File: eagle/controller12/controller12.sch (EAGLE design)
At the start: 60 parts, among them IC1 ILD213T, J2 AVR_SPI_PRG_62X3_LOCK, Q1 FDD4141TO252, Q2 200mA/50V, Q3 FDD4141TO252, Q4 200mA/50V, Q5 200mA/50V, U3 MP2307, X1 1501_04, X2 ZX62D-B-5PA8

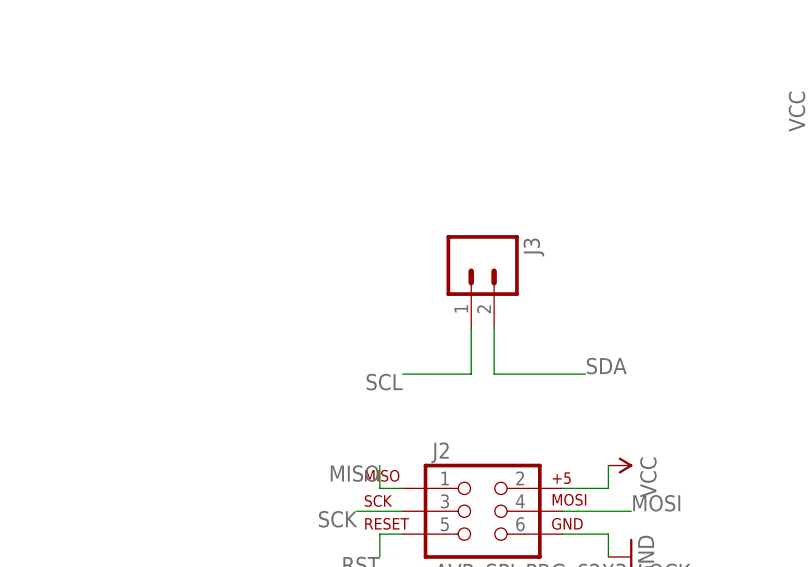
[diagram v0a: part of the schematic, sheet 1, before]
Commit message: controller12: added header for possible extension board
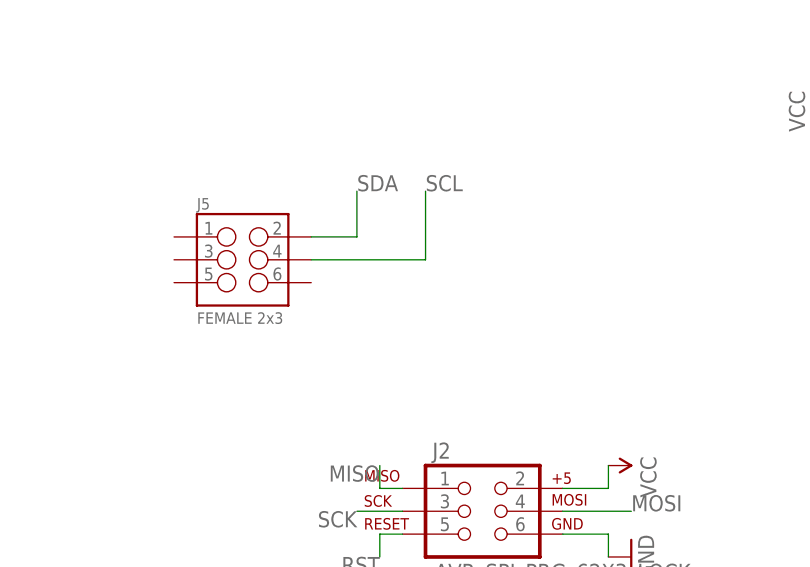
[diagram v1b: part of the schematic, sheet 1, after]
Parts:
- removed J3: (no value), SparkFun-Connectors:M02LOCK
- added J5: FEMALE 2x3, SparkFun-Connectors:M03X2FEMALE
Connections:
- net SCL: no longer J3.1
- net SDA: no longer J3.2
- net Z_GPIO_1: no longer J1.2
- net Z_GPIO_2: no longer J1.4
- net Z_GPIO_3: no longer J1.6
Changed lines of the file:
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@@
 <part name="S2" library="SparkFun-Electromechanical" deviceset="SWITCH-SPDT" device="SMD2"/>
 <part name="SUPPLY8" library="SparkFun-Aesthetics" deviceset="VCC" device=""/>
-<part name="J3" library="SparkFun-Connectors" deviceset="M02" device="LOCK"/>
+<part name="J5" library="SparkFun-Connectors" deviceset="M03X2" device="FEMALE" value="FEMALE 2x3"/>
 </parts>
 <sheets>
@@
 <instance part="S2" gate="1" x="162.56" y="106.68"/>
 <instance part="SUPPLY8" gate="G$1" x="147.32" y="106.68" rot="R90"/>
-<instance part="J3" gate="G$1" x="106.68" y="91.44" rot="R270"/>
+<instance part="J5" gate="G$1" x="81.28" y="91.44"/>
 </instances>
 <busses>
@@
 </segment>
 <segment>
-<wire x1="106.68" y1="78.74" x2="99.06" y2="78.74" width="0.1524" layer="91"/>
-<label x="99.06" y="78.74" size="1.778" layer="95" rot="R180"/>
-<pinref part="J3" gate="G$1" pin="1"/>
-<wire x1="106.68" y1="78.74" x2="106.68" y2="83.82" width="0.1524" layer="91"/>
+<wire x1="101.6" y1="91.44" x2="101.6" y2="99.06" width="0.1524" layer="91"/>
+<label x="101.6" y="99.06" size="1.778" layer="95"/>
+<wire x1="101.6" y1="91.44" x2="88.9" y2="91.44" width="0.1524" layer="91"/>
 </segment>
 </net>
@@
 </segment>
 <segment>
-<wire x1="109.22" y1="78.74" x2="119.38" y2="78.74" width="0.1524" layer="91"/>
-<label x="119.38" y="78.74" size="1.778" layer="95"/>
-<pinref part="J3" gate="G$1" pin="2"/>
-<wire x1="109.22" y1="78.74" x2="109.22" y2="83.82" width="0.1524" layer="91"/>
+<wire x1="93.98" y1="93.98" x2="93.98" y2="99.06" width="0.1524" layer="91"/>
+<label x="93.98" y="99.06" size="1.778" layer="95"/>
+<wire x1="93.98" y1="93.98" x2="88.9" y2="93.98" width="0.1524" layer="91"/>
 </segment>
 </net>
@@
 </segment>
 </net>
-<net name="Z_GPIO_1" class="0">
-<segment>
-<pinref part="J1" gate="G$1" pin="2"/>
-<wire x1="88.9" y1="73.66" x2="101.6" y2="73.66" width="0.1524" layer="91"/>
-<label x="101.6" y="73.66" size="1.778" layer="95"/>
-</segment>
-</net>
-<net name="Z_GPIO_2" class="0">
-<segment>
-<pinref part="J1" gate="G$1" pin="4"/>
-<wire x1="88.9" y1="71.12" x2="101.6" y2="71.12" width="0.1524" layer="91"/>
-<label x="101.6" y="71.12" size="1.778" layer="95"/>
-</segment>
-</net>
-<net name="Z_GPIO_3" class="0">
-<segment>
-<pinref part="J1" gate="G$1" pin="6"/>
-<wire x1="88.9" y1="68.58" x2="101.6" y2="68.58" width="0.1524" layer="91"/>
-<label x="101.6" y="68.58" size="1.778" layer="95"/>
-</segment>
-</net>

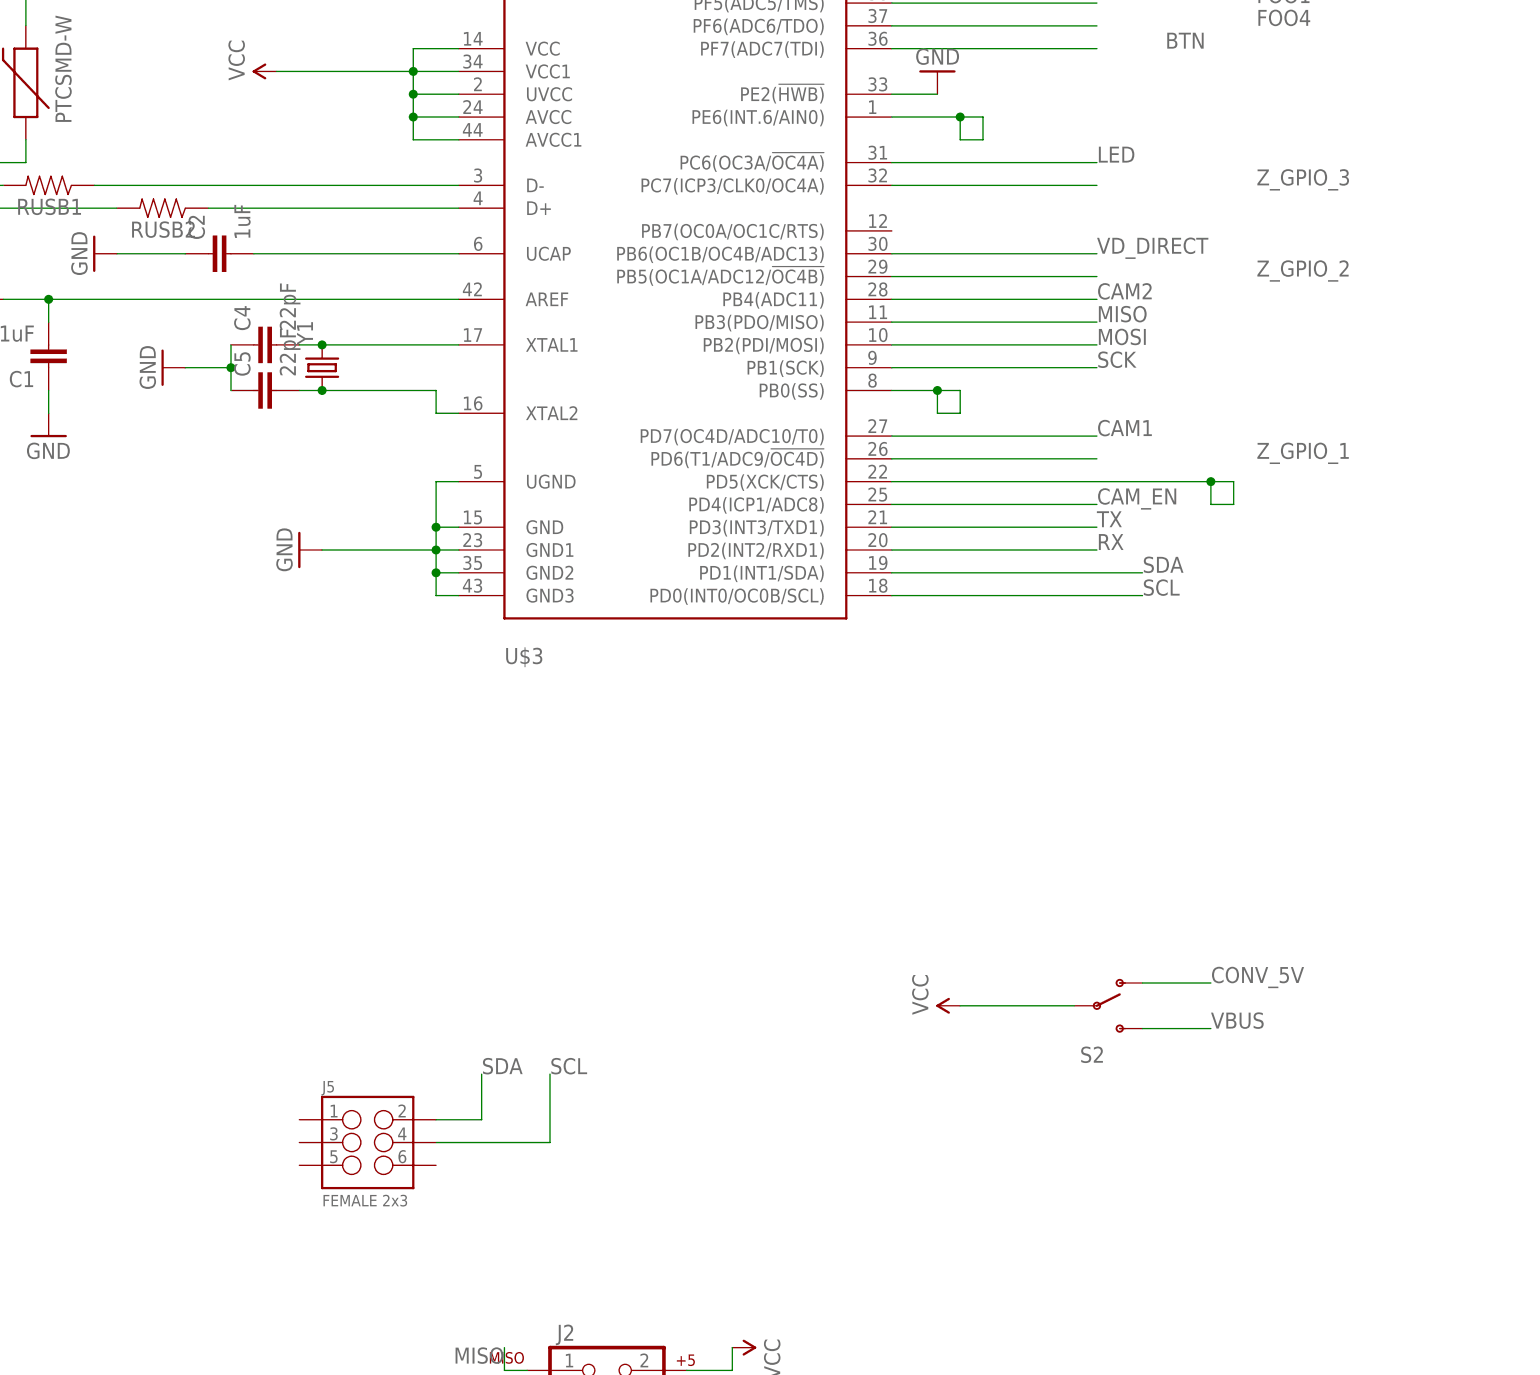
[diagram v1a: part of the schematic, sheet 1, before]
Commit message: controller12 routing improved
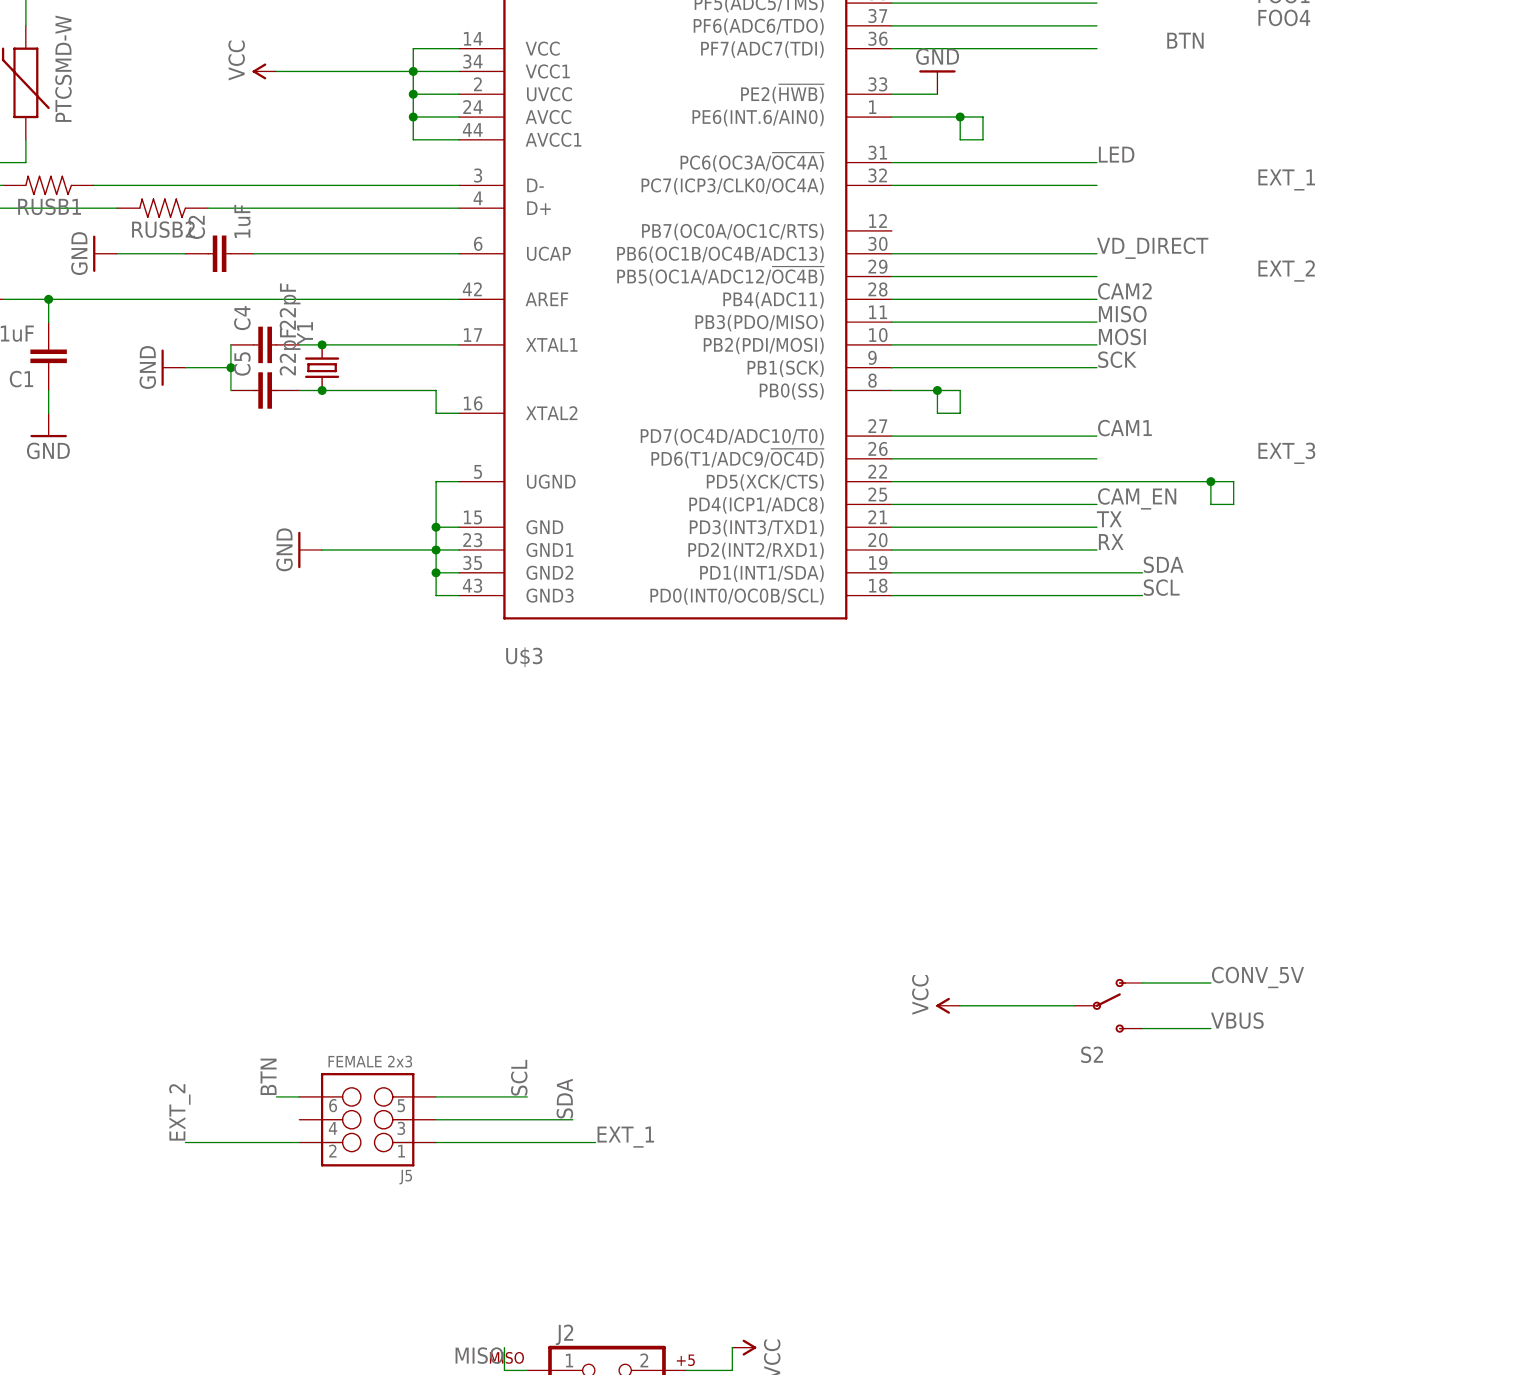
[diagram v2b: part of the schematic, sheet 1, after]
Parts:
- J4: device SparkFun-Connectors:M02LOCK -> SparkFun-Connectors:M02PTH
- S1: device SparkFun-Retired:TAC_SWITCHSMD -> SparkFun-Retired:TAC_SWITCHPTH
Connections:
- net Z_GPIO_1 renamed EXT_3
- removed net Z_GPIO_2: U$3.PB5(OC1A/ADC12/!OC4B)
- removed net Z_GPIO_3: U$3.PC7(ICP3/CLK0/OC4A)
- new net EXT_1: J5.1, U$3.PC7(ICP3/CLK0/OC4A)
- new net EXT_2: J5.2, U$3.PB5(OC1A/ADC12/!OC4B)
- net BTN: now also J5.6
- net SCL: now also J5.5
- net SDA: now also J5.3
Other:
- moved on the sheet: J5

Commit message: controller 12 progress zero_standalone enclosure
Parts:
- added D1: MBRS130LT3, diode:MBRS130LT3
- J2: value AVR_SPI_PRG_62X3_LOCK -> AVR_SPI_PRG_6PTH; device SparkFun-Connectors:AVR_SPI_PRG_62X3_LOCK -> SparkFun-Connectors:AVR_SPI_PRG_6PTH
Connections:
- removed net EXT_3: U$3.PD6(T1/ADC9/!OC4D)
- new net FOO5: U$3.PF7(ADC7(TDI)
- net BTN: now also J5.4, S1.4, U$3.PD6(T1/ADC9/!OC4D); no longer J5.6, S1.3, U$3.PF7(ADC7(TDI)
- net GND: now also J5.6
- net GNDA: now also D1.A
- net N$26: now also D1.C
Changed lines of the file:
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@@
 <part name="U$4" library="volzolib" deviceset="NANOFIT2" device=""/>
 <part name="U$5" library="volzolib" deviceset="NANOFIT2" device=""/>
-<part name="J2" library="SparkFun-Connectors" deviceset="AVR_SPI_PRG_6" device="2X3_LOCK"/>
+<part name="J2" library="SparkFun-Connectors" deviceset="AVR_SPI_PRG_6" device="PTH" value="AVR_SPI_PRG_6PTH"/>
 <part name="J4" library="SparkFun-Connectors" deviceset="M02" device="PTH"/>
 <part name="GND7" library="SparkFun-Aesthetics" deviceset="GND" device=""/>
@@
 <part name="SUPPLY8" library="SparkFun-Aesthetics" deviceset="VCC" device=""/>
 <part name="J5" library="SparkFun-Connectors" deviceset="M03X2" device="FEMALE" value="FEMALE 2x3"/>
+<part name="GND21" library="SparkFun-Aesthetics" deviceset="GND" device=""/>
+<part name="D1" library="diode" library_urn="urn:adsk.eagle:library:210" deviceset="MBRS130LT3" device="" package3d_urn="urn:adsk.eagle:package:43404/2"/>
+<part name="GND23" library="supply1" library_urn="urn:adsk.eagle:library:371" deviceset="GNDA" device=""/>
 </parts>
 <sheets>
@@
 <instance part="SUPPLY8" gate="G$1" x="147.32" y="106.68" rot="R90"/>
 <instance part="J5" gate="G$1" x="81.28" y="93.98" rot="R180"/>
+<instance part="GND21" gate="1" x="71.12" y="101.6" rot="R180"/>
 </instances>
 <busses>
@@
 <pinref part="GND29" gate="1" pin="GND"/>
 </segment>
+<segment>
+<pinref part="J5" gate="G$1" pin="6"/>
+<pinref part="GND21" gate="1" pin="GND"/>
+<wire x1="73.66" y1="96.52" x2="71.12" y2="96.52" width="0.1524" layer="91"/>
+<wire x1="71.12" y1="96.52" x2="71.12" y2="99.06" width="0.1524" layer="91"/>
+</segment>
 </net>
 <net name="RX" class="0">
@@
 <net name="BTN" class="0">
 <segment>
-<pinref part="S1" gate="S" pin="3"/>
 <pinref part="R5" gate="G$1" pin="2"/>
-<wire x1="58.42" y1="22.86" x2="66.04" y2="22.86" width="0.1524" layer="91"/>
 <wire x1="66.04" y1="22.86" x2="76.2" y2="22.86" width="0.1524" layer="91"/>
+<label x="76.2" y="22.86" size="1.778" layer="95"/>
+<pinref part="S1" gate="S" pin="4"/>
+<wire x1="58.42" y1="20.32" x2="63.5" y2="20.32" width="0.1524" layer="91"/>
+<wire x1="63.5" y1="20.32" x2="63.5" y2="22.86" width="0.1524" layer="91"/>
+<wire x1="63.5" y1="22.86" x2="66.04" y2="22.86" width="0.1524" layer="91"/>
 <junction x="66.04" y="22.86"/>
-<label x="76.2" y="22.86" size="1.778" layer="95"/>
-</segment>
-<segment>
-<pinref part="U$3" gate="G$1" pin="PF7(ADC7(TDI)"/>
-<wire x1="139.7" y1="213.36" x2="162.56" y2="213.36" width="0.1524" layer="91"/>
-<label x="170.18" y="213.36" size="1.778" layer="95"/>
-</segment>
-<segment>
-<pinref part="J5" gate="G$1" pin="6"/>
-<wire x1="73.66" y1="96.52" x2="71.12" y2="96.52" width="0.1524" layer="91"/>
-<label x="71.12" y="96.52" size="1.778" layer="95" rot="R90"/>
+</segment>
+<segment>
+<pinref part="U$3" gate="G$1" pin="PD6(T1/ADC9/!OC4D)"/>
+<wire x1="139.7" y1="167.64" x2="162.56" y2="167.64" width="0.1524" layer="91"/>
+<label x="180.34" y="167.64" size="1.778" layer="95"/>
+</segment>
+<segment>
+<pinref part="J5" gate="G$1" pin="4"/>
+<wire x1="73.66" y1="93.98" x2="66.04" y2="93.98" width="0.1524" layer="91"/>
+<label x="66.04" y="93.98" size="1.778" layer="95" rot="R90"/>
 </segment>
 </net>
@@
 </segment>
 </net>
-<net name="EXT_3" class="0">
-<segment>
-<pinref part="U$3" gate="G$1" pin="PD6(T1/ADC9/!OC4D)"/>
-<wire x1="139.7" y1="167.64" x2="162.56" y2="167.64" width="0.1524" layer="91"/>
-<label x="180.34" y="167.64" size="1.778" layer="95"/>
-</segment>
-</net>
 <net name="VBUS" class="0">
 <segment>
@@
 <wire x1="139.7" y1="187.96" x2="162.56" y2="187.96" width="0.1524" layer="91"/>
 <label x="180.34" y="187.96" size="1.778" layer="95"/>
+</segment>
+</net>
+<net name="FOO5" class="0">
+<segment>
+<pinref part="U$3" gate="G$1" pin="PF7(ADC7(TDI)"/>
+<wire x1="139.7" y1="213.36" x2="162.56" y2="213.36" width="0.1524" layer="91"/>
+<label x="180.34" y="213.36" size="1.778" layer="95"/>
 </segment>
 </net>
@@
 <instance part="J4" gate="G$1" x="172.72" y="111.76"/>
 <instance part="GND7" gate="1" x="198.12" y="114.3" rot="R90"/>
+<instance part="D1" gate="G$1" x="144.78" y="203.2" rot="R270"/>
+<instance part="GND23" gate="1" x="144.78" y="213.36" rot="R180"/>
 </instances>
 <busses>
@@
 <segment>
 <pinref part="U3" gate="G$1" pin="3"/>
-<wire x1="157.48" y1="223.52" x2="147.32" y2="223.52" width="0.1524" layer="91"/>
-<wire x1="147.32" y1="223.52" x2="147.32" y2="195.58" width="0.1524" layer="91"/>
-<wire x1="147.32" y1="195.58" x2="152.4" y2="195.58" width="0.1524" layer="91"/>
+<wire x1="157.48" y1="223.52" x2="139.7" y2="223.52" width="0.1524" layer="91"/>
+<wire x1="139.7" y1="223.52" x2="139.7" y2="195.58" width="0.1524" layer="91"/>
+<wire x1="139.7" y1="195.58" x2="144.78" y2="195.58" width="0.1524" layer="91"/>
 <pinref part="C13" gate="G$1" pin="2"/>
+<wire x1="144.78" y1="195.58" x2="152.4" y2="195.58" width="0.1524" layer="91"/>
 <wire x1="152.4" y1="195.58" x2="157.48" y2="195.58" width="0.1524" layer="91"/>
 <wire x1="152.4" y1="200.66" x2="152.4" y2="195.58" width="0.1524" layer="91"/>
 <junction x="152.4" y="195.58"/>
 <pinref part="L2" gate="G$1" pin="2"/>
+<pinref part="D1" gate="G$1" pin="C"/>
+<wire x1="144.78" y1="195.58" x2="144.78" y2="200.66" width="0.1524" layer="91"/>
+<junction x="144.78" y="195.58"/>
 </segment>
 </net>
@@
 <pinref part="GND17" gate="1" pin="GNDA"/>
 </segment>
+<segment>
+<pinref part="D1" gate="G$1" pin="A"/>
+<wire x1="144.78" y1="205.74" x2="144.78" y2="210.82" width="0.1524" layer="91"/>
+<pinref part="GND23" gate="1" pin="GNDA"/>
+</segment>
 </net>
 </nets>
@@
 with this version.
 </note>
+<note version="8.3" severity="warning">
+Since Version 8.3, EAGLE supports URNs for individual library
+assets (packages, symbols, and devices). The URNs of those assets
+will not be understood (or retained) with this version.
+</note>
+<note version="8.3" severity="warning">
+Since Version 8.3, EAGLE supports the association of 3D packages
+with devices in libraries, schematics, and board files. Those 3D
+packages will not be understood (or retained) with this version.
+</note>
 </compatibility>
